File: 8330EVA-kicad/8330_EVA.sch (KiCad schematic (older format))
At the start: 0 parts

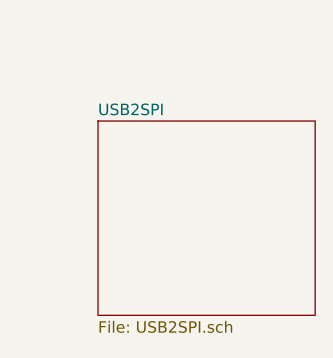
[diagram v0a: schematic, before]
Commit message: 完成FT232驱动电路原理图的绘制，并未相关的元件添加了封装
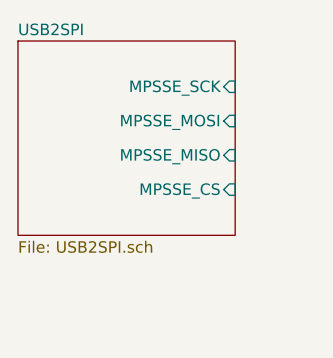
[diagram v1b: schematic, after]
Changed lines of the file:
@@
 EESchema Schematic File Version 4
+LIBS:8330_EVA-cache
 EELAYER 29 0
 EELAYER END
@@
 $EndDescr
 $Sheet
-S 3050 2250 950  850
+S 2700 1900 950  850
 U 5BEE3A6A
 F0 "USB2SPI" 50
 F1 "USB2SPI.sch" 50
+F2 "MPSSE_SCK" I R 3650 2100 50
+F3 "MPSSE_MOSI" I R 3650 2250 50
+F4 "MPSSE_MISO" I R 3650 2400 50
+F5 "MPSSE_CS" I R 3650 2550 50
 $EndSheet
 $EndSCHEMATC

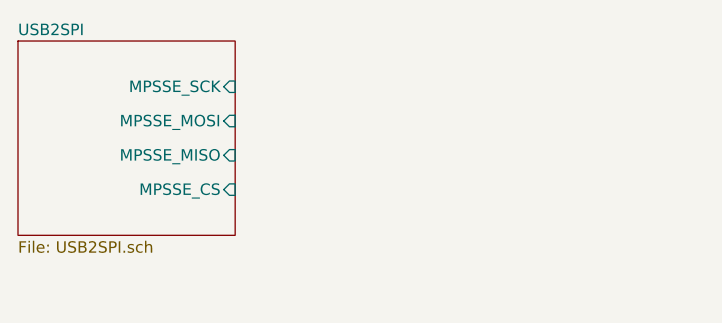
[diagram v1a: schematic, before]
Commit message: add symbol/package of AD8131 and AD8330
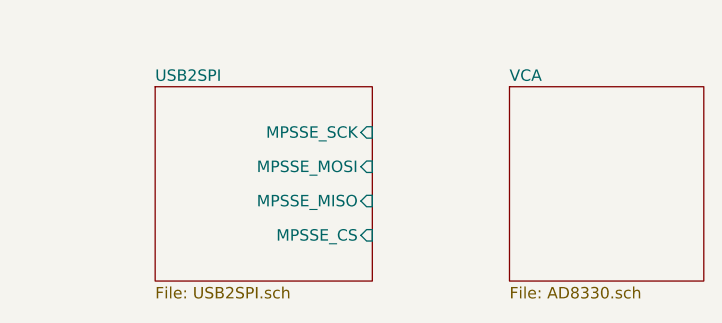
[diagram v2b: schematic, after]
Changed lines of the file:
@@
 $Descr A4 11693 8268
 encoding utf-8
-Sheet 1 2
+Sheet 1 3
 Title ""
 Date ""
@@
 $EndDescr
 $Sheet
-S 2700 1900 950  850
+S 3300 2100 950  850
 U 5BEE3A6A
 F0 "USB2SPI" 50
 F1 "USB2SPI.sch" 50
-F2 "MPSSE_SCK" I R 3650 2100 50
-F3 "MPSSE_MOSI" I R 3650 2250 50
-F4 "MPSSE_MISO" I R 3650 2400 50
-F5 "MPSSE_CS" I R 3650 2550 50
+F2 "MPSSE_SCK" I R 4250 2300 50
+F3 "MPSSE_MOSI" I R 4250 2450 50
+F4 "MPSSE_MISO" I R 4250 2600 50
+F5 "MPSSE_CS" I R 4250 2750 50
+$EndSheet
+$Sheet
+S 4850 2100 850  850
+U 5BF7C1D8
+F0 "VCA" 50
+F1 "AD8330.sch" 50
 $EndSheet
 $EndSCHEMATC

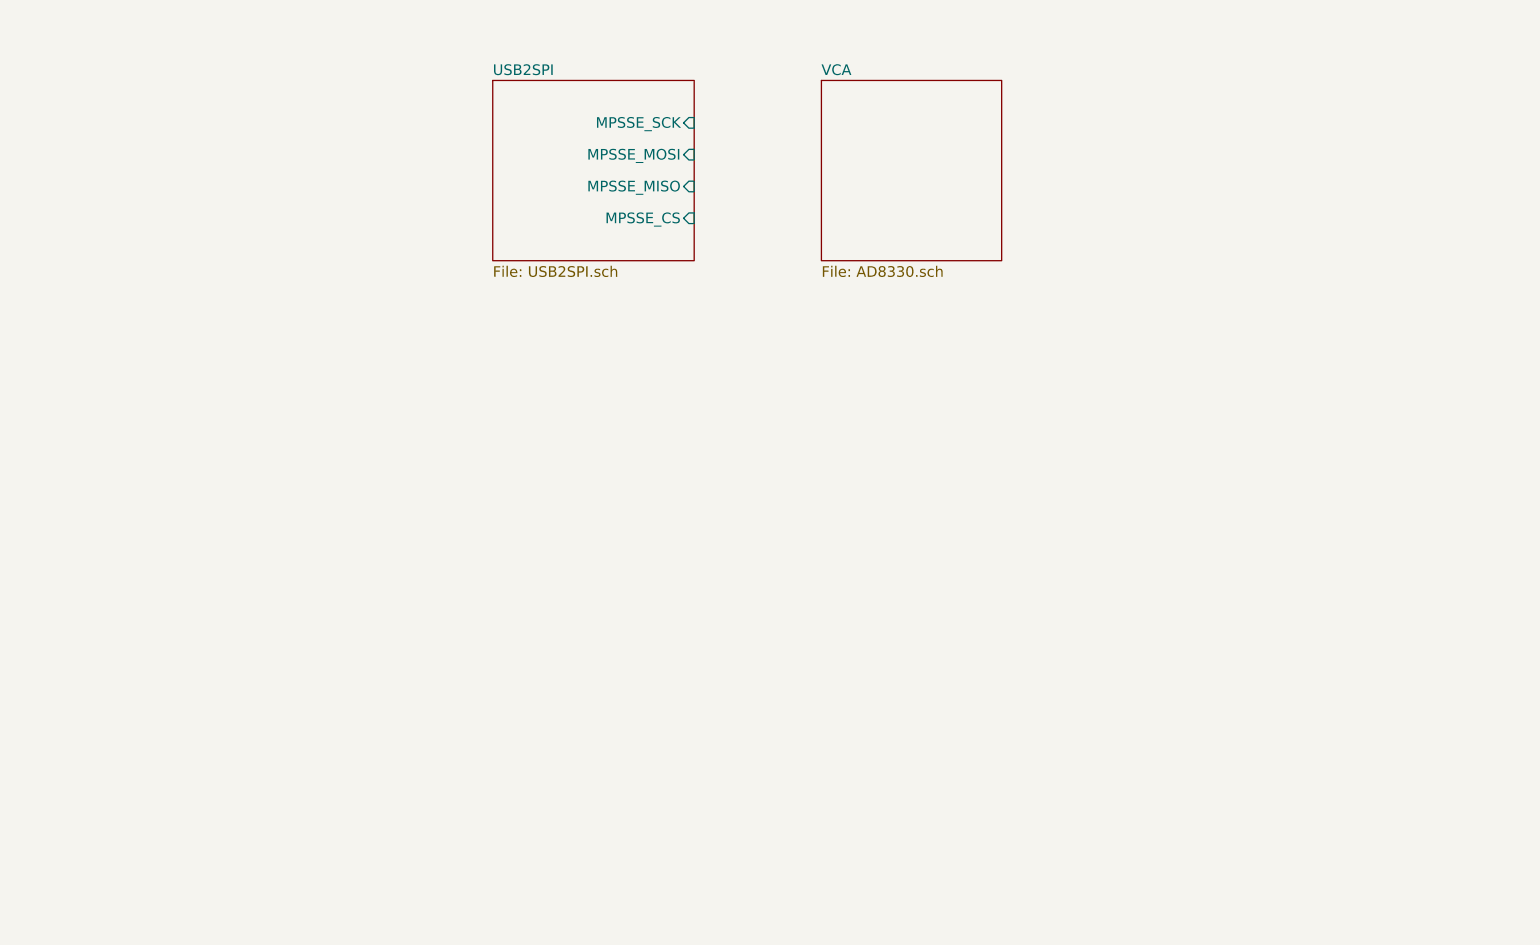
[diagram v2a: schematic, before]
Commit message: 完成AD8330 VGA电路原理图的绘制
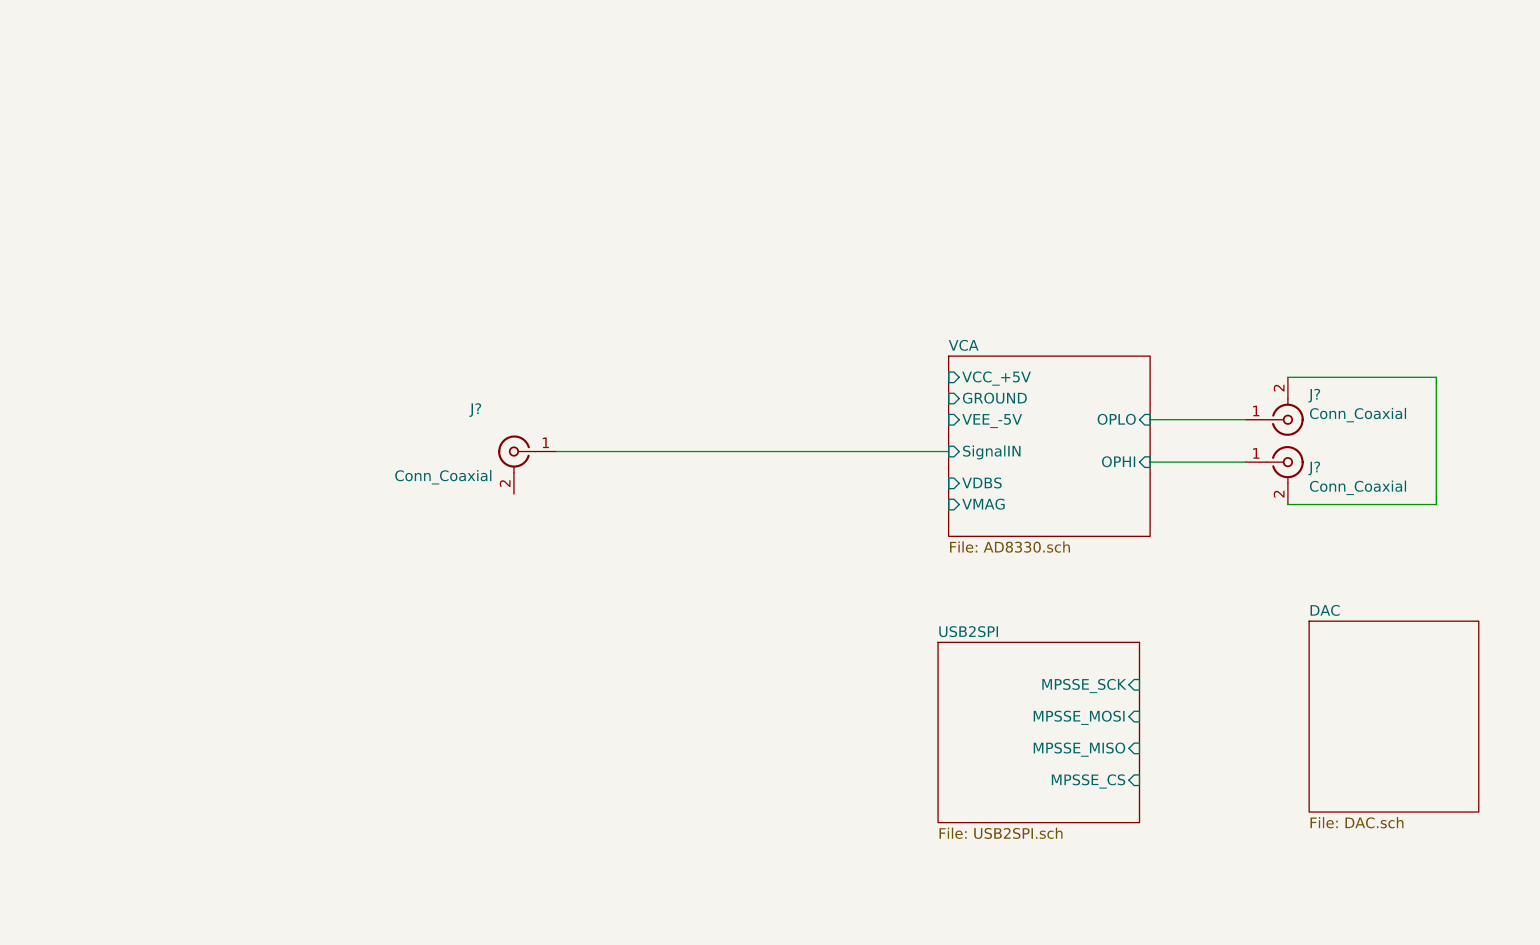
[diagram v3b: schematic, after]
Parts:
- added J? (x3): Conn_Coaxial, symbol Connector:Conn_Coaxial
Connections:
- new net: J?.2 (Ext), J?.2 (Ext)
- new net VCA/OPHI: J?.1 (In)
- new net VCA/OPLO: J?.1 (In)
- new net VCA/SignalIN: J?.1 (In)
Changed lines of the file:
@@
 $Descr A4 11693 8268
 encoding utf-8
-Sheet 1 3
+Sheet 1 5
 Title ""
 Date ""
@@
 $EndDescr
 $Sheet
-S 3300 2100 950  850
+S 5400 4750 950  850
 U 5BEE3A6A
 F0 "USB2SPI" 50
 F1 "USB2SPI.sch" 50
-F2 "MPSSE_SCK" I R 4250 2300 50
-F3 "MPSSE_MOSI" I R 4250 2450 50
-F4 "MPSSE_MISO" I R 4250 2600 50
-F5 "MPSSE_CS" I R 4250 2750 50
+F2 "MPSSE_SCK" I R 6350 4950 50
+F3 "MPSSE_MOSI" I R 6350 5100 50
+F4 "MPSSE_MISO" I R 6350 5250 50
+F5 "MPSSE_CS" I R 6350 5400 50
 $EndSheet
 $Sheet
-S 4850 2100 850  850
+S 5450 3400 950  850
 U 5BF7C1D8
 F0 "VCA" 50
 F1 "AD8330.sch" 50
+F2 "OPLO" I R 6400 3700 50
+F3 "OPHI" I R 6400 3900 50
+F4 "VMAG" I L 5450 4100 50
+F5 "VDBS" I L 5450 4000 50
+F6 "VCC_+5V" I L 5450 3500 50
+F7 "VEE_-5V" I L 5450 3700 50
+F8 "GROUND" I L 5450 3600 50
+F9 "SignalIN" I L 5450 3850 50
 $EndSheet
+$Comp
+L Connector:Conn_Coaxial J?
+U 1 1 5BF938E3
+P 3400 3850
+F 0 "J?" H 3550 4050 50  0000 L CNN
+F 1 "Conn_Coaxial" H 3500 3734 50  0000 L CNN
+F 2 "" H 3400 3850 50  0001 C CNN
+F 3 " ~" H 3400 3850 50  0001 C CNN
+	1    3400 3850
+	-1   0    0    -1
+$EndComp
+$Comp
+L Connector:Conn_Coaxial J?
+U 1 1 5BF93FB8
+P 7050 3700
+F 0 "J?" H 7150 3582 50  0000 L CNN
+F 1 "Conn_Coaxial" H 7150 3673 50  0000 L CNN
+F 2 "" H 7050 3700 50  0001 C CNN
+F 3 " ~" H 7050 3700 50  0001 C CNN
+	1    7050 3700
+	1    0    0    1
+$EndComp
+$Comp
+L Connector:Conn_Coaxial J?
+U 1 1 5BF9438D
+P 7050 3900
+F 0 "J?" H 7150 3875 50  0000 L CNN
+F 1 "Conn_Coaxial" H 7150 3784 50  0000 L CNN
+F 2 "" H 7050 3900 50  0001 C CNN
+F 3 " ~" H 7050 3900 50  0001 C CNN
+	1    7050 3900
+	1    0    0    -1
+$EndComp
+$Sheet
+S 7150 4650 800  900
+U 5BF9AAF9
+F0 "DAC" 50
+F1 "DAC.sch" 50
+$EndSheet
+Wire Wire Line
+	6850 3900 6400 3900
+Wire Wire Line
+	6400 3700 6850 3700
+Wire Wire Line
+	7050 4100 7750 4100
+Wire Wire Line
+	7750 4100 7750 3500
+Wire Wire Line
+	7750 3500 7050 3500
+Wire Wire Line
+	3600 3850 5450 3850
 $EndSCHEMATC

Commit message: 添加DAC部分/修改FT232供电方式（原理图）
1. 完成AD5312及REF192组成的程控信号产生部分原理图绘制
2. 修改FT232H的供电方式，添加了3.3VLDO，从之前的BUS-Power改为Self_Power
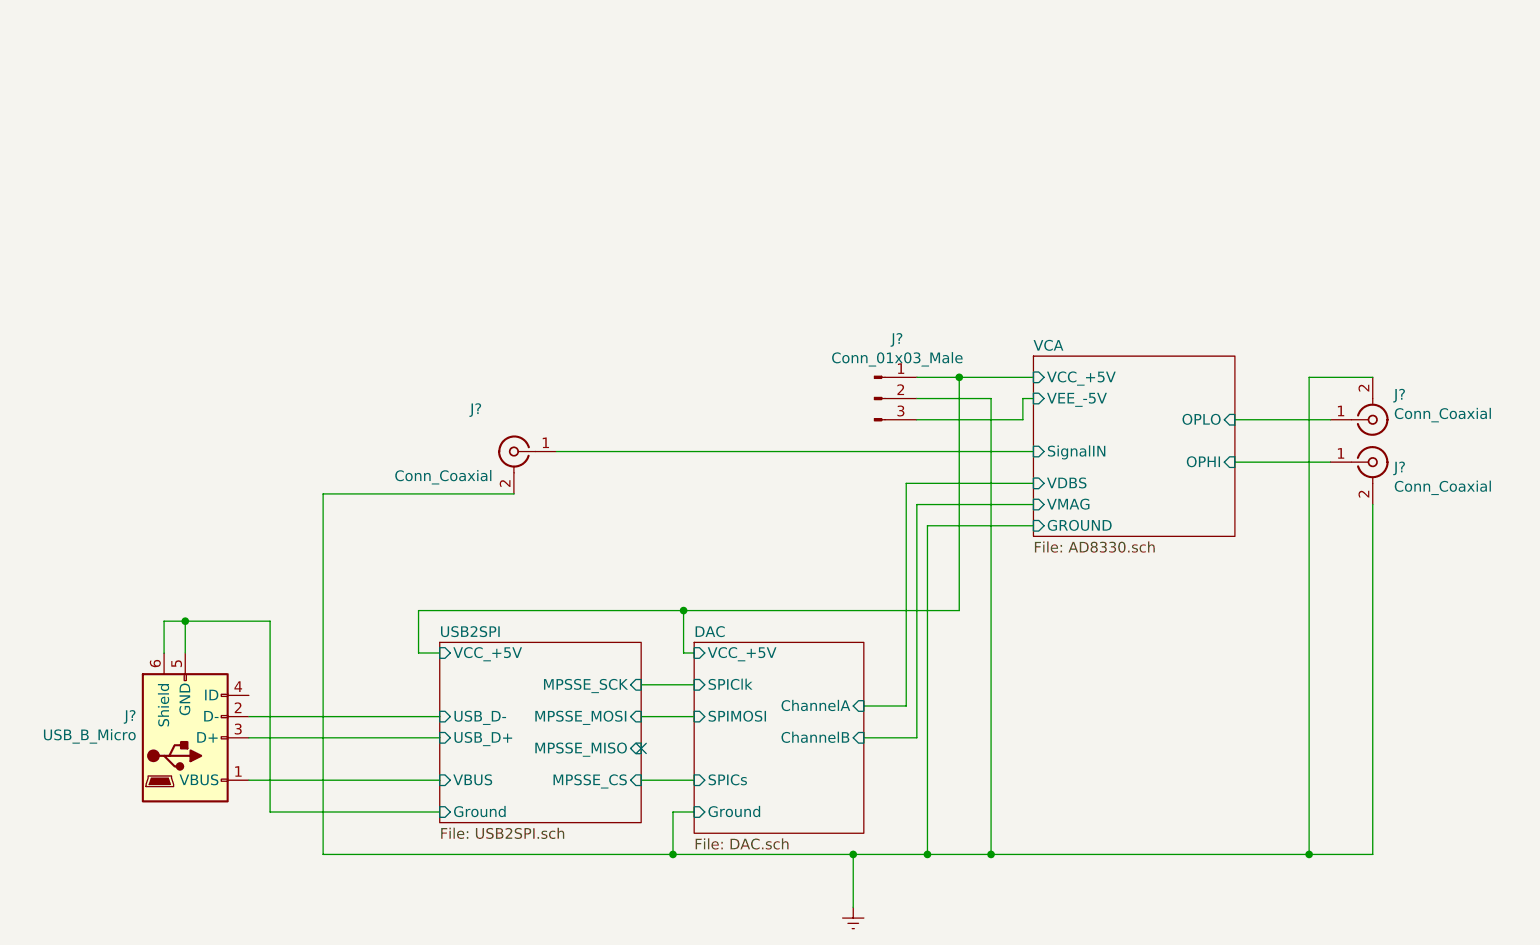
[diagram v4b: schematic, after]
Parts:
- added J?: Conn_01x03_Male, symbol Connector:Conn_01x03_Male
- added J?: USB_B_Micro, Connector_USB:USB_Micro-B_Wuerth_614105150721_Vertical, symbol Connector:USB_B_Micro
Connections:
- net VCA/VEE_-5V: now also J?.3 (Pin_3)
- net Earth: now reaches J?.2 (Ext)
- net Earth: now also J?.2 (Ext), J?.2 (Ext), J?.2 (Pin_2)
- new net DAC/VCC_+5V: J?.1 (Pin_1)
- new net USB2SPI/Ground: J?.5 (GND), J?.6 (Shield)
- new net USB2SPI/USB_D+: J?.3 (D+)
- new net USB2SPI/USB_D-: J?.2 (D-)
- new net USB2SPI/VBUS: J?.1 (VBUS)
- no-connect marks 0 -> 1
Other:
- moved on the sheet: J?
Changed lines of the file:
@@
 $EndDescr
 $Sheet
-S 5400 4750 950  850
+S 3050 4750 950  850
 U 5BEE3A6A
 F0 "USB2SPI" 50
 F1 "USB2SPI.sch" 50
-F2 "MPSSE_SCK" I R 6350 4950 50
-F3 "MPSSE_MOSI" I R 6350 5100 50
-F4 "MPSSE_MISO" I R 6350 5250 50
-F5 "MPSSE_CS" I R 6350 5400 50
+F2 "MPSSE_SCK" I R 4000 4950 50
+F3 "MPSSE_MOSI" I R 4000 5100 50
+F4 "MPSSE_MISO" I R 4000 5250 50
+F5 "MPSSE_CS" I R 4000 5400 50
+F6 "USB_D+" I L 3050 5200 50
+F7 "USB_D-" I L 3050 5100 50
+F8 "VBUS" I L 3050 5400 50
+F9 "Ground" I L 3050 5550 50
+F10 "VCC_+5V" I L 3050 4800 50
 $EndSheet
 $Sheet
-S 5450 3400 950  850
+S 5850 3400 950  850
 U 5BF7C1D8
 F0 "VCA" 50
 F1 "AD8330.sch" 50
-F2 "OPLO" I R 6400 3700 50
-F3 "OPHI" I R 6400 3900 50
-F4 "VMAG" I L 5450 4100 50
-F5 "VDBS" I L 5450 4000 50
-F6 "VCC_+5V" I L 5450 3500 50
-F7 "VEE_-5V" I L 5450 3700 50
-F8 "GROUND" I L 5450 3600 50
-F9 "SignalIN" I L 5450 3850 50
+F2 "OPLO" I R 6800 3700 50
+F3 "OPHI" I R 6800 3900 50
+F4 "VMAG" I L 5850 4100 50
+F5 "VDBS" I L 5850 4000 50
+F6 "VCC_+5V" I L 5850 3500 50
+F7 "VEE_-5V" I L 5850 3600 50
+F8 "GROUND" I L 5850 4200 50
+F9 "SignalIN" I L 5850 3850 50
 $EndSheet
 $Comp
@@
 L Connector:Conn_Coaxial J?
 U 1 1 5BF93FB8
-P 7050 3700
-F 0 "J?" H 7150 3582 50  0000 L CNN
-F 1 "Conn_Coaxial" H 7150 3673 50  0000 L CNN
-F 2 "" H 7050 3700 50  0001 C CNN
-F 3 " ~" H 7050 3700 50  0001 C CNN
-	1    7050 3700
+P 7450 3700
+F 0 "J?" H 7550 3582 50  0000 L CNN
+F 1 "Conn_Coaxial" H 7550 3673 50  0000 L CNN
+F 2 "" H 7450 3700 50  0001 C CNN
+F 3 " ~" H 7450 3700 50  0001 C CNN
+	1    7450 3700
 	1    0    0    1
 $EndComp
@@
 L Connector:Conn_Coaxial J?
 U 1 1 5BF9438D
-P 7050 3900
-F 0 "J?" H 7150 3875 50  0000 L CNN
-F 1 "Conn_Coaxial" H 7150 3784 50  0000 L CNN
-F 2 "" H 7050 3900 50  0001 C CNN
-F 3 " ~" H 7050 3900 50  0001 C CNN
-	1    7050 3900
+P 7450 3900
+F 0 "J?" H 7550 3875 50  0000 L CNN
+F 1 "Conn_Coaxial" H 7550 3784 50  0000 L CNN
+F 2 "" H 7450 3900 50  0001 C CNN
+F 3 " ~" H 7450 3900 50  0001 C CNN
+	1    7450 3900
 	1    0    0    -1
 $EndComp
 $Sheet
-S 7150 4650 800  900
+S 4250 4750 800  900
 U 5BF9AAF9
 F0 "DAC" 50
 F1 "DAC.sch" 50
+F2 "VCC_+5V" I L 4250 4800 50
+F3 "SPIClk" I L 4250 4950 50
+F4 "SPIMOSI" I L 4250 5100 50
+F5 "ChannelA" I R 5050 5050 50
+F6 "ChannelB" I R 5050 5200 50
+F7 "SPICs" I L 4250 5400 50
+F8 "Ground" I L 4250 5550 50
 $EndSheet
 Wire Wire Line
-	6850 3900 6400 3900
-Wire Wire Line
-	6400 3700 6850 3700
-Wire Wire Line
-	7050 4100 7750 4100
-Wire Wire Line
-	7750 4100 7750 3500
-Wire Wire Line
-	7750 3500 7050 3500
-Wire Wire Line
-	3600 3850 5450 3850
+	7250 3900 6800 3900
+Wire Wire Line
+	6800 3700 7250 3700
+Wire Wire Line
+	4250 4950 4000 4950
+Wire Wire Line
+	4250 5100 4000 5100
+Wire Wire Line
+	4250 5400 4000 5400
+Wire Wire Line
+	5050 5050 5250 5050
+Wire Wire Line
+	5250 5050 5250 4000
+Wire Wire Line
+	5300 4100 5300 5200
+Wire Wire Line
+	5300 5200 5050 5200
+NoConn ~ 4000 5250
+Wire Wire Line
+	5350 4200 5350 5750
+Wire Wire Line
+	5350 5750 5000 5750
+Wire Wire Line
+	4250 5550 4150 5550
+Wire Wire Line
+	4150 5550 4150 5750
+Wire Wire Line
+	3400 4050 2500 4050
+Wire Wire Line
+	2500 4050 2500 5750
+Wire Wire Line
+	2500 5750 4150 5750
+Connection ~ 4150 5750
+Connection ~ 5350 5750
+$Comp
+L power:Earth #PWR?
+U 1 1 5C0E471A
+P 5000 6000
+F 0 "#PWR?" H 5000 5750 50  0001 C CNN
+F 1 "Earth" H 5000 5850 50  0001 C CNN
+F 2 "" H 5000 6000 50  0001 C CNN
+F 3 "~" H 5000 6000 50  0001 C CNN
+	1    5000 6000
+	1    0    0    -1
+$EndComp
+Wire Wire Line
+	5000 6000 5000 5750
+Connection ~ 5000 5750
+Wire Wire Line
+	5000 5750 4150 5750
+$Comp
+L Connector:Conn_01x03_Male J?
+U 1 1 5C0E5EB0
+P 5100 3600
+F 0 "J?" H 5208 3881 50  0000 C CNN
+F 1 "Conn_01x03_Male" H 5208 3790 50  0000 C CNN
+F 2 "" H 5100 3600 50  0001 C CNN
+F 3 "~" H 5100 3600 50  0001 C CNN
+	1    5100 3600
+	1    0    0    -1
+$EndComp
+Wire Wire Line
+	3600 3850 5850 3850
+Wire Wire Line
+	5250 4000 5850 4000
+Wire Wire Line
+	5300 4100 5850 4100
+Wire Wire Line
+	5350 4200 5850 4200
+Wire Wire Line
+	5300 3500 5500 3500
+Wire Wire Line
+	5300 3700 5800 3700
+Wire Wire Line
+	5800 3700 5800 3600
+Wire Wire Line
+	5800 3600 5850 3600
+Wire Wire Line
+	5300 3600 5650 3600
+Wire Wire Line
+	5650 3600 5650 5750
+Connection ~ 5650 5750
+Wire Wire Line
+	5650 5750 5350 5750
+Wire Wire Line
+	7450 4100 7450 5750
+Wire Wire Line
+	5650 5750 7150 5750
+Wire Wire Line
+	7450 3500 7150 3500
+Wire Wire Line
+	7150 3500 7150 5750
+Connection ~ 7150 5750
+Wire Wire Line
+	7150 5750 7450 5750
+$Comp
+L Connector:USB_B_Micro J?
+U 1 1 5C0F0C42
+P 1850 5200
+AR Path="/5BEE3A6A/5C0F0C42" Ref="J?"  Part="1"
+AR Path="/5C0F0C42" Ref="J?"  Part="1"
+F 0 "J?" H 1620 5097 50  0000 R CNN
+F 1 "USB_B_Micro" H 1620 5188 50  0000 R CNN
+F 2 "Connector_USB:USB_Micro-B_Wuerth_614105150721_Vertical" H 2000 5150 50  0001 C CNN
+F 3 "~" H 2000 5150 50  0001 C CNN
+	1    1850 5200
+	1    0    0    1
+$EndComp
+Wire Wire Line
+	3050 4800 2950 4800
+Wire Wire Line
+	2950 4800 2950 4600
+Wire Wire Line
+	2950 4600 4200 4600
+Wire Wire Line
+	4200 4600 4200 4800
+Wire Wire Line
+	4200 4800 4250 4800
+Wire Wire Line
+	5500 3500 5500 4600
+Wire Wire Line
+	5500 4600 4200 4600
+Connection ~ 5500 3500
+Wire Wire Line
+	5500 3500 5850 3500
+Connection ~ 4200 4600
+Wire Wire Line
+	3050 5100 2150 5100
+Wire Wire Line
+	2150 5200 3050 5200
+Wire Wire Line
+	3050 5400 2150 5400
+Wire Wire Line
+	2250 5550 3050 5550
+Wire Wire Line
+	1750 4800 1750 4650
+Wire Wire Line
+	1750 4650 1850 4650
+Wire Wire Line
+	1850 4650 1850 4800
+Wire Wire Line
+	1850 4650 2250 4650
+Wire Wire Line
+	2250 4650 2250 5550
+Connection ~ 1850 4650
 $EndSCHEMATC

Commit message: 修复若干ERC未连接错误
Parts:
- gave numbers to parts that had none: 5
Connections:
- no-connect marks 1 -> 2
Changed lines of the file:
@@
 $EndSheet
 $Comp
-L Connector:Conn_Coaxial J?
+L Connector:Conn_Coaxial J2
 U 1 1 5BF938E3
 P 3400 3850
-F 0 "J?" H 3550 4050 50  0000 L CNN
+F 0 "J2" H 3550 4050 50  0000 L CNN
 F 1 "Conn_Coaxial" H 3500 3734 50  0000 L CNN
 F 2 "" H 3400 3850 50  0001 C CNN
@@
 $EndComp
 $Comp
-L Connector:Conn_Coaxial J?
+L Connector:Conn_Coaxial J4
 U 1 1 5BF93FB8
 P 7450 3700
-F 0 "J?" H 7550 3582 50  0000 L CNN
+F 0 "J4" H 7550 3582 50  0000 L CNN
 F 1 "Conn_Coaxial" H 7550 3673 50  0000 L CNN
 F 2 "" H 7450 3700 50  0001 C CNN
@@
 $EndComp
 $Comp
-L Connector:Conn_Coaxial J?
+L Connector:Conn_Coaxial J5
 U 1 1 5BF9438D
 P 7450 3900
-F 0 "J?" H 7550 3875 50  0000 L CNN
+F 0 "J5" H 7550 3875 50  0000 L CNN
 F 1 "Conn_Coaxial" H 7550 3784 50  0000 L CNN
 F 2 "" H 7450 3900 50  0001 C CNN
@@
 Connection ~ 5350 5750
 $Comp
-L power:Earth #PWR?
+L power:Earth #PWR0101
 U 1 1 5C0E471A
 P 5000 6000
-F 0 "#PWR?" H 5000 5750 50  0001 C CNN
+F 0 "#PWR0101" H 5000 5750 50  0001 C CNN
 F 1 "Earth" H 5000 5850 50  0001 C CNN
 F 2 "" H 5000 6000 50  0001 C CNN
@@
 	5000 5750 4150 5750
 $Comp
-L Connector:Conn_01x03_Male J?
+L Connector:Conn_01x03_Male J3
 U 1 1 5C0E5EB0
 P 5100 3600
-F 0 "J?" H 5208 3881 50  0000 C CNN
+F 0 "J3" H 5208 3881 50  0000 C CNN
 F 1 "Conn_01x03_Male" H 5208 3790 50  0000 C CNN
 F 2 "" H 5100 3600 50  0001 C CNN
@@
 P 1850 5200
 AR Path="/5BEE3A6A/5C0F0C42" Ref="J?"  Part="1"
-AR Path="/5C0F0C42" Ref="J?"  Part="1"
-F 0 "J?" H 1620 5097 50  0000 R CNN
+AR Path="/5C0F0C42" Ref="J1"  Part="1"
+F 0 "J1" H 1620 5097 50  0000 R CNN
 F 1 "USB_B_Micro" H 1620 5188 50  0000 R CNN
 F 2 "Connector_USB:USB_Micro-B_Wuerth_614105150721_Vertical" H 2000 5150 50  0001 C CNN
@@
 	2250 4650 2250 5550
 Connection ~ 1850 4650
+NoConn ~ 2150 5000
 $EndSCHEMATC

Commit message: 为变压器制作封装
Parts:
- J2, J4, J5: footprint (none) -> Connector_Coaxial:SMA_Amphenol_132289_EdgeMount
- J3: footprint (none) -> Connector_PinHeader_2.54mm:PinHeader_1x03_P2.54mm_Vertical
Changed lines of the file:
@@
 F 0 "J2" H 3550 4050 50  0000 L CNN
 F 1 "Conn_Coaxial" H 3500 3734 50  0000 L CNN
-F 2 "" H 3400 3850 50  0001 C CNN
+F 2 "Connector_Coaxial:SMA_Amphenol_132289_EdgeMount" H 3400 3850 50  0001 C CNN
 F 3 " ~" H 3400 3850 50  0001 C CNN
 	1    3400 3850
@@
 F 0 "J4" H 7550 3582 50  0000 L CNN
 F 1 "Conn_Coaxial" H 7550 3673 50  0000 L CNN
-F 2 "" H 7450 3700 50  0001 C CNN
+F 2 "Connector_Coaxial:SMA_Amphenol_132289_EdgeMount" H 7450 3700 50  0001 C CNN
 F 3 " ~" H 7450 3700 50  0001 C CNN
 	1    7450 3700
@@
 F 0 "J5" H 7550 3875 50  0000 L CNN
 F 1 "Conn_Coaxial" H 7550 3784 50  0000 L CNN
-F 2 "" H 7450 3900 50  0001 C CNN
+F 2 "Connector_Coaxial:SMA_Amphenol_132289_EdgeMount" H 7450 3900 50  0001 C CNN
 F 3 " ~" H 7450 3900 50  0001 C CNN
 	1    7450 3900
@@
 F 0 "J3" H 5208 3881 50  0000 C CNN
 F 1 "Conn_01x03_Male" H 5208 3790 50  0000 C CNN
-F 2 "" H 5100 3600 50  0001 C CNN
+F 2 "Connector_PinHeader_2.54mm:PinHeader_1x03_P2.54mm_Vertical" H 5100 3600 50  0001 C CNN
 F 3 "~" H 5100 3600 50  0001 C CNN
 	1    5100 3600
